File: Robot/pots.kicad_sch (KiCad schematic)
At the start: 8 parts

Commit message: Started PCB roughting
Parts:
- C51: renamed from C48; footprint (none) -> Capacitor_SMD:C_1210_3225Metric_Pad1.33x2.70mm_HandSolder
- C52: renamed from C49; footprint (none) -> Capacitor_SMD:C_0603_1608Metric_Pad1.08x0.95mm_HandSolder
- C53: renamed from C50; footprint (none) -> Capacitor_SMD:C_0603_1608Metric_Pad1.08x0.95mm_HandSolder
- C54: renamed from C51; footprint (none) -> Capacitor_SMD:C_0603_1608Metric_Pad1.08x0.95mm_HandSolder
- R53: renamed from R46; footprint (none) -> Resistor_SMD:R_0603_1608Metric_Pad0.98x0.95mm_HandSolder
- renumbered R43 to R54, R44 to R55, R45 to R56
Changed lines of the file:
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@@
 		(dnp no)
 		(fields_autoplaced yes)
-		(property "Reference" "R44"
+		(property "Reference" "R55"
 			(at 146.05 96.5199 90)
 			(effects
@@
 			(project "Robot"
 				(path "/c5aa62e4-5f59-48a4-ae5d-57fc70429dc3/7a01a313-5403-4786-9812-b769a17d4656"
-					(reference "R44")
+					(reference "R55")
 					(unit 1)
 				)
@@
 		(dnp no)
 		(fields_autoplaced yes)
-		(property "Reference" "R43"
+		(property "Reference" "R54"
 			(at 113.03 96.5199 90)
 			(effects
@@
 			(project "Robot"
 				(path "/c5aa62e4-5f59-48a4-ae5d-57fc70429dc3/7a01a313-5403-4786-9812-b769a17d4656"
-					(reference "R43")
+					(reference "R54")
 					(unit 1)
 				)
@@
 		(dnp no)
 		(fields_autoplaced yes)
-		(property "Reference" "C51"
+		(property "Reference" "C54"
 			(at 195.58 126.9999 0)
 			(effects
@@
 			)
 		)
-		(property "Footprint" ""
+		(property "Footprint" "Capacitor_SMD:C_0603_1608Metric_Pad1.08x0.95mm_HandSolder"
 			(at 190.8048 124.46 0)
 			(effects
@@
 			(project "Robot"
 				(path "/c5aa62e4-5f59-48a4-ae5d-57fc70429dc3/7a01a313-5403-4786-9812-b769a17d4656"
-					(reference "C51")
+					(reference "C54")
 					(unit 1)
 				)
@@
 		(dnp no)
 		(fields_autoplaced yes)
-		(property "Reference" "C49"
+		(property "Reference" "C52"
 			(at 130.81 126.9999 0)
 			(effects
@@
 			)
 		)
-		(property "Footprint" ""
+		(property "Footprint" "Capacitor_SMD:C_0603_1608Metric_Pad1.08x0.95mm_HandSolder"
 			(at 126.0348 124.46 0)
 			(effects
@@
 			(project "Robot"
 				(path "/c5aa62e4-5f59-48a4-ae5d-57fc70429dc3/7a01a313-5403-4786-9812-b769a17d4656"
-					(reference "C49")
+					(reference "C52")
 					(unit 1)
 				)
@@
 		(dnp no)
 		(fields_autoplaced yes)
-		(property "Reference" "C50"
+		(property "Reference" "C53"
 			(at 161.29 126.9999 0)
 			(effects
@@
 			)
 		)
-		(property "Footprint" ""
+		(property "Footprint" "Capacitor_SMD:C_0603_1608Metric_Pad1.08x0.95mm_HandSolder"
 			(at 156.5148 124.46 0)
 			(effects
@@
 			(project "Robot"
 				(path "/c5aa62e4-5f59-48a4-ae5d-57fc70429dc3/7a01a313-5403-4786-9812-b769a17d4656"
-					(reference "C50")
+					(reference "C53")
 					(unit 1)
 				)
@@
 		(dnp no)
 		(fields_autoplaced yes)
-		(property "Reference" "#PWR098"
+		(property "Reference" "#PWR0104"
 			(at 95.25 81.28 0)
 			(effects
@@
 			(project "Robot"
 				(path "/c5aa62e4-5f59-48a4-ae5d-57fc70429dc3/7a01a313-5403-4786-9812-b769a17d4656"
-					(reference "#PWR098")
+					(reference "#PWR0104")
 					(unit 1)
 				)
@@
 		(dnp no)
 		(fields_autoplaced yes)
-		(property "Reference" "#PWR099"
+		(property "Reference" "#PWR0106"
 			(at 127 147.32 0)
 			(effects
@@
 			(project "Robot"
 				(path "/c5aa62e4-5f59-48a4-ae5d-57fc70429dc3/7a01a313-5403-4786-9812-b769a17d4656"
-					(reference "#PWR099")
+					(reference "#PWR0106")
 					(unit 1)
 				)
@@
 		(dnp no)
 		(fields_autoplaced yes)
-		(property "Reference" "#PWR097"
+		(property "Reference" "#PWR0103"
 			(at 120.65 68.58 0)
 			(effects
@@
 			(project "Robot"
 				(path "/c5aa62e4-5f59-48a4-ae5d-57fc70429dc3/7a01a313-5403-4786-9812-b769a17d4656"
-					(reference "#PWR097")
+					(reference "#PWR0103")
 					(unit 1)
 				)
@@
 		(dnp no)
 		(fields_autoplaced yes)
-		(property "Reference" "R45"
+		(property "Reference" "R56"
 			(at 180.34 96.5199 90)
 			(effects
@@
 			(project "Robot"
 				(path "/c5aa62e4-5f59-48a4-ae5d-57fc70429dc3/7a01a313-5403-4786-9812-b769a17d4656"
-					(reference "R45")
+					(reference "R56")
 					(unit 1)
 				)
@@
 		(dnp no)
 		(fields_autoplaced yes)
-		(property "Reference" "R46"
+		(property "Reference" "R53"
 			(at 123.19 72.3899 0)
 			(effects
@@
 			)
 		)
-		(property "Footprint" ""
+		(property "Footprint" "Resistor_SMD:R_0603_1608Metric_Pad0.98x0.95mm_HandSolder"
 			(at 118.872 73.66 90)
 			(effects
@@
 			(project "Robot"
 				(path "/c5aa62e4-5f59-48a4-ae5d-57fc70429dc3/7a01a313-5403-4786-9812-b769a17d4656"
-					(reference "R46")
+					(reference "R53")
 					(unit 1)
 				)
@@
 		(dnp no)
 		(fields_autoplaced yes)
-		(property "Reference" "#PWR096"
+		(property "Reference" "#PWR0105"
 			(at 120.65 119.38 0)
 			(effects
@@
 			(project "Robot"
 				(path "/c5aa62e4-5f59-48a4-ae5d-57fc70429dc3/7a01a313-5403-4786-9812-b769a17d4656"
-					(reference "#PWR096")
+					(reference "#PWR0105")
 					(unit 1)
 				)
@@
 		(dnp no)
 		(fields_autoplaced yes)
-		(property "Reference" "C48"
+		(property "Reference" "C51"
 			(at 111.76 73.66 90)
 			(effects
@@
 			)
 		)
-		(property "Footprint" ""
+		(property "Footprint" "Capacitor_SMD:C_1210_3225Metric_Pad1.33x2.70mm_HandSolder"
 			(at 115.57 80.3148 0)
 			(effects
@@
 			(project "Robot"
 				(path "/c5aa62e4-5f59-48a4-ae5d-57fc70429dc3/7a01a313-5403-4786-9812-b769a17d4656"
-					(reference "C48")
-					(unit 1)
-				)
+					(reference "C51")
+					(unit 1)
+				)

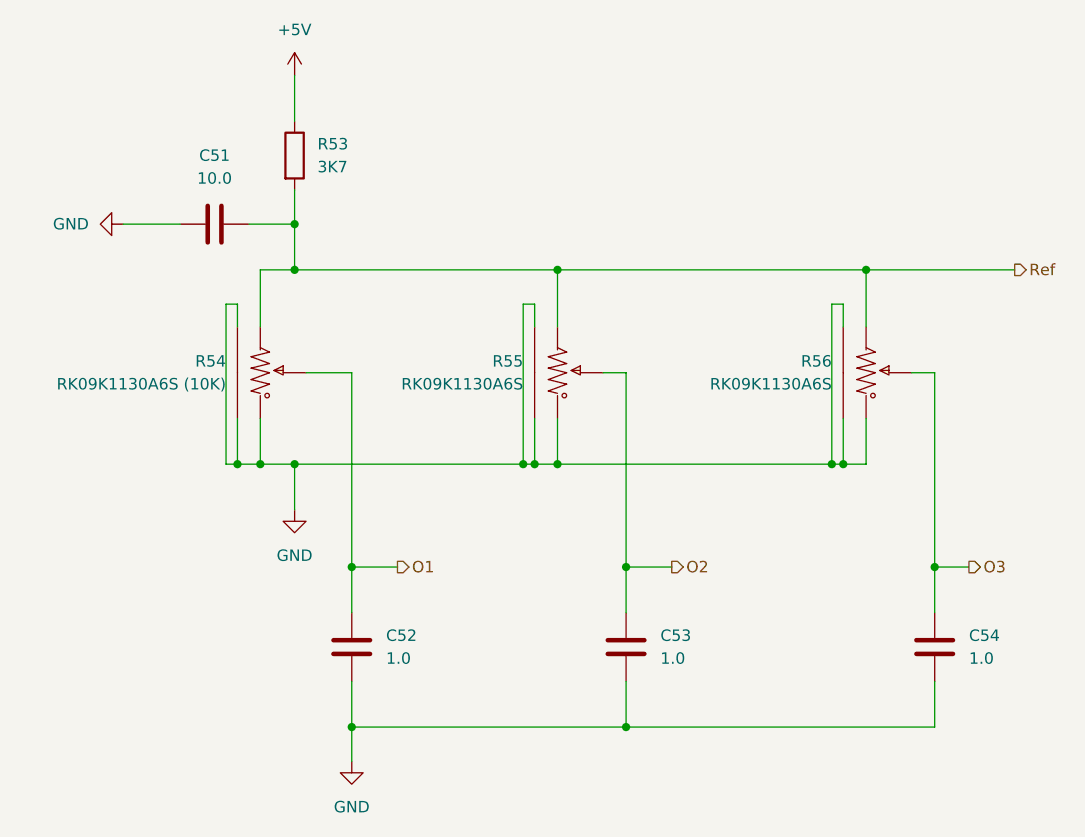
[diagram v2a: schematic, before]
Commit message: Updated SCH & PCB for Robot
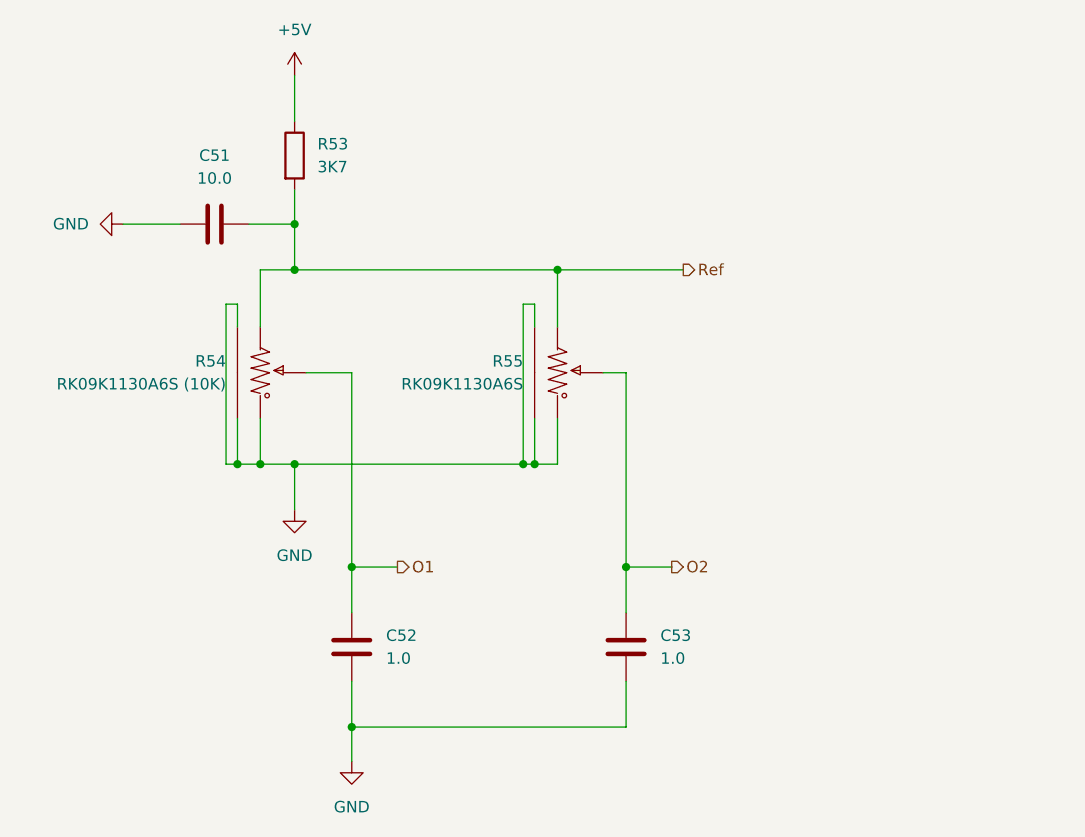
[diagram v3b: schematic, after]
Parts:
- removed C54: 1.0, Capacitor_SMD:C_0603_1608Metric_Pad1.08x0.95mm_HandSolder, symbol Device:C
- removed R56: RK09K1130A6S, easyeda2kicad:RES-TH_RK09K1130A6S, symbol easyeda2kicad:RK09K1130A6S

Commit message: Updated PCB & Patterns for Robot
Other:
- company: (none) -> RoboWay
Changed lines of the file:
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@@
 	(generator_version "9.0")
 	(paper "A4")
+	(title_block
+		(company "RoboWay")
+	)
 	(junction
 		(at 149.86 86.36)
